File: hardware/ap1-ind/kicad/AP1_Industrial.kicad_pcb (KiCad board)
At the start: 2 copper layers, 88 x 56 mm, 71 parts, among them J1 ENTRADA 12-24V, J2 CONTACTORES, J3 0-10V, J7 PROGRAMADOR, Q1 AO3400A, Q2 AO3400A, U1 LMR16006XDDC, U2 B1212S-1WR3, U3 LM358DR2G, U4 LM358DR2G, U5 M24C02-WMN6TP

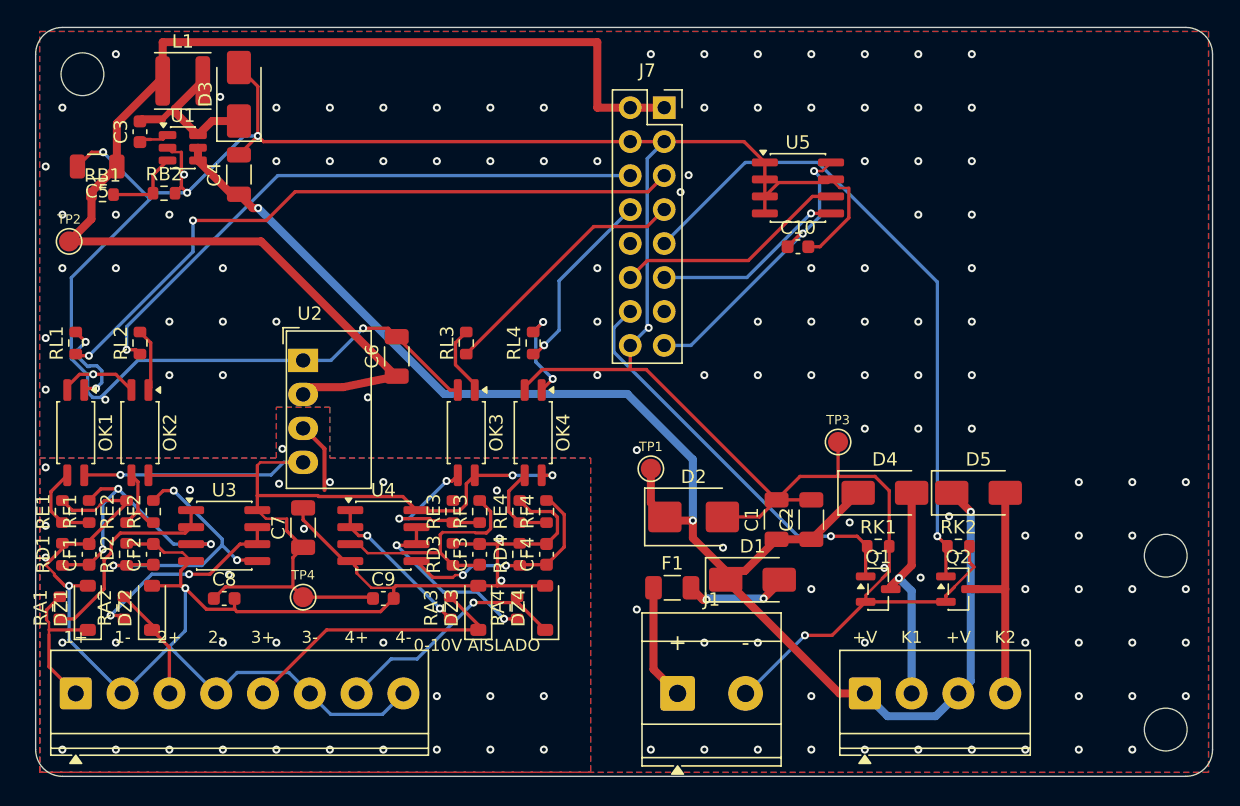
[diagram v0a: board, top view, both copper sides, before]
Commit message: Listo para JLCPCB: códigos LCSC, reglas de fabricación y carpeta de pedido
- Códigos LCSC verificados para todas las piezas SMD (INA238, LMR16006,
  UCC27524, AL8860, TMP1075, MOSFET, bobinas, capacitor, fusible, módulo,
  conectores) en tools/jlcpcb.py; piezas reconocidas por huella.
- Shunt: el WSK2512 de 4 terminales se agotó en LCSC; base y AP-0.2 usan un
  HoJLR2512 1 mOhm 2 W (C2924520) con huella propia 'net tie' que conserva
  el sensado Kelvin (tools/huellas/LetreroLab.pretty).
- ESP32-C3-WROOM-02: huella propia con 4 vías de 0.3 mm en lugar de 12 de
  0.2 mm (proceso estándar de JLCPCB). Textos de serigrafía de 0.8 mm o más.
- IND: fusible de 3 A (el mismo de la base).
- AP-0.2 ruteada otra vez con el nuevo shunt.
- Las 4 placas: ERC 0, DRC 0, 0 sin conectar, 0 diferencias y 0 problemas
  con las reglas de fabricación de JLCPCB.
- PEDIDO_JLCPCB/ (+ .zip) con Gerber, BOM y CPL completos o solo SMD por
  placa, y PEDIDO_JLCPCB.md con las opciones exactas del pedido.

Co-Authored-By: Claude Opus 5.5 <noreply@anthropic.com>
Claude-Session: https://claude.ai/code/session_01WVk3oGwfQfGTmAT2PMp8oW
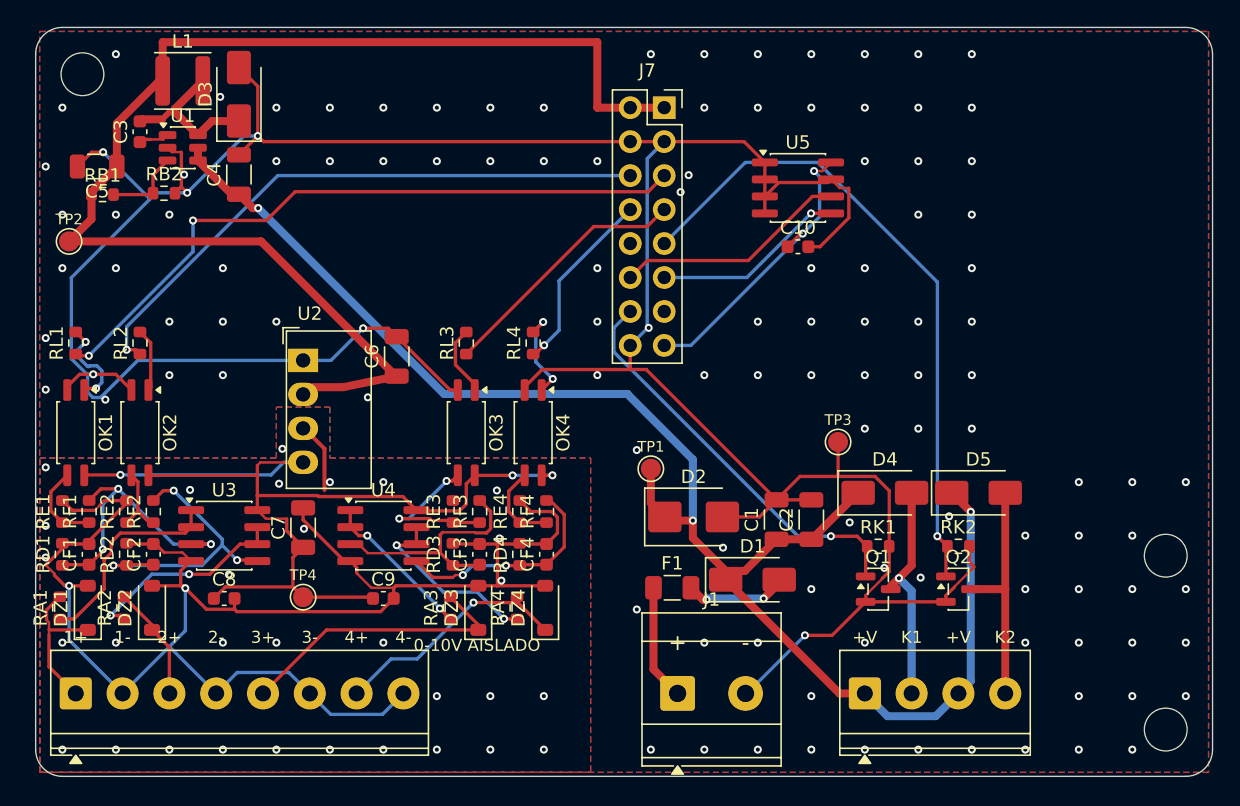
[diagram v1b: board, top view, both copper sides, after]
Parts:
- F1: value 2A -> 3A
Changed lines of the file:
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@@
 			)
 		)
-		(property "Value" "2A"
+		(property "Value" "3A"
 			(at 0 1.83 0)
 			(layer "F.Fab")
@@
 			(effects
 				(font
-					(size 0.7 0.7)
-					(thickness 0.12)
+					(size 0.8 0.8)
+					(thickness 0.15)
 				)
 			)
@@
 			(effects
 				(font
-					(size 0.7 0.7)
-					(thickness 0.12)
+					(size 0.8 0.8)
+					(thickness 0.15)
 				)
 			)
@@
 			(effects
 				(font
-					(size 0.7 0.7)
-					(thickness 0.12)
+					(size 0.8 0.8)
+					(thickness 0.15)
 				)
 			)
@@
 			(effects
 				(font
-					(size 0.7 0.7)
-					(thickness 0.12)
+					(size 0.8 0.8)
+					(thickness 0.15)
 				)
 			)

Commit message: AP CONNECT: sin borneras en todas las placas, placa nueva AP PRO AI4 y guía de fabricantes
- Borneras de tornillo reemplazadas por conectores con cable y código LCSC verificado:
  XT60 (C98732), JST VH 2/3/4 (C160315/6/7), JST XH 2/3/4 (C158012, C144394/5), Qwiic
  en BASE, IND, PIX, DMX, PLANTILLA, AP INPUT, AP OUTPUT y DIST 4; zonas de potencia rehechas
- XT60 de la DIST 4 con la polaridad marcada en la huella (pata 1 = -, pata 2 = +)
- TCA9554PWR ya con código (C477924)
- ap1-ai4: 4 entradas 0-10 V / 4-20 mA con ADS1115 (C37593), +24 V para sensores de lazo
- Programa 1.7: lectura AI4, umbrales con acciones, Home Assistant, tarjeta en la app
- FABRICANTES.md: JLCPCB, PCBWay, Seeed, NextPCB, México; impresión 3D y tornillería
- Pedido JLCPCB con 10 placas (AP-0.2 retirada); ERC/DRC/DFM 0 en todas

Co-Authored-By: Claude Opus 5.5 <noreply@anthropic.com>
Claude-Session: https://claude.ai/code/session_01WVk3oGwfQfGTmAT2PMp8oW
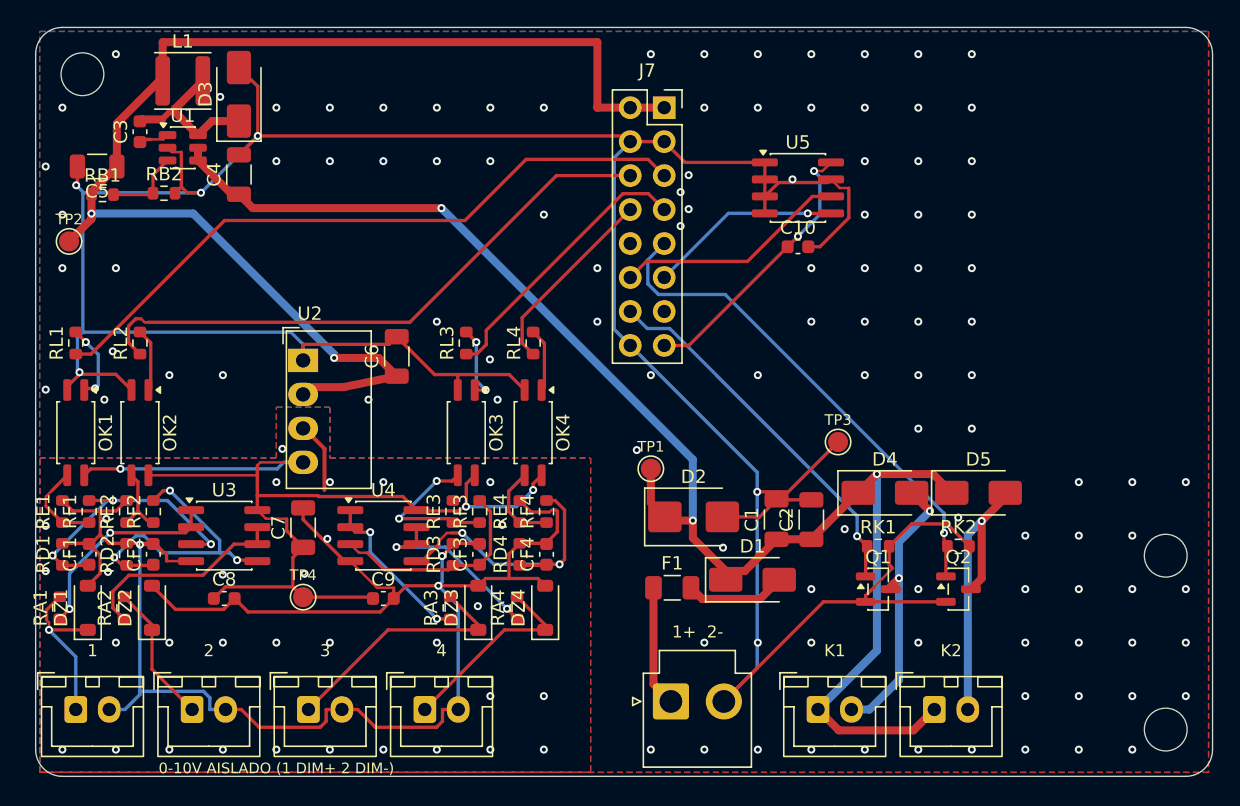
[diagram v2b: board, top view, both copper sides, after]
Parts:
- removed J3: 0-10V, TerminalBlock_Phoenix:TerminalBlock_Phoenix_PT-1,5-8-3.5-H_1x08_P3.50mm_Horizontal
- added J4: K2, Connector_JST:JST_XH_B2B-XH-A_1x02_P2.50mm_Vertical, F.Cu at (167.2, 151.0)
- added J5: 0-10V 1, Connector_JST:JST_XH_B2B-XH-A_1x02_P2.50mm_Vertical, F.Cu at (103.0, 151.0)
- added J6: 0-10V 2, Connector_JST:JST_XH_B2B-XH-A_1x02_P2.50mm_Vertical, F.Cu at (111.7, 151.0)
- added J8: 0-10V 3, Connector_JST:JST_XH_B2B-XH-A_1x02_P2.50mm_Vertical, F.Cu at (120.4, 151.0)
- added J9: 0-10V 4, Connector_JST:JST_XH_B2B-XH-A_1x02_P2.50mm_Vertical, F.Cu at (129.1, 151.0)
- J1: footprint TerminalBlock_Phoenix:TerminalBlock_Phoenix_MKDS-3-2-5.08_1x02_P5.08mm_Horizontal -> Connector_JST:JST_VH_B2P-VH_1x02_P3.96mm_Vertical
- J2: value CONTACTORES -> K1; footprint TerminalBlock_Phoenix:TerminalBlock_Phoenix_PT-1,5-4-3.5-H_1x04_P3.50mm_Horizontal -> Connector_JST:JST_XH_B2B-XH-A_1x02_P2.50mm_Vertical
- moved J2 3.70 mm to (158.5, 151.0)
- moved J1 0.78 mm to (147.5, 150.4)
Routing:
- net /CC1: track 49.0 -> 37.6 mm
- net /ISOGND: track 129.9 -> 140.2 mm, vias 33 -> 35
- net /GND: track 234.6 -> 240.5 mm, vias 119 -> 112
- net /K2: track 17.6 -> 22.8 mm, vias 0 -> 1
- net /FL4: track 16.7 -> 21.6 mm
- net /K1: track 16.9 -> 21.1 mm, vias 1 -> 2
- net /DIM4: track 18.2 -> 14.8 mm, vias 1 -> 0
- net /DIM3: track 21.4 -> 18.5 mm
- net /AUX: track 30.8 -> 28.2 mm
- net /LA4: track 7.25 -> 4.77 mm, vias 2 -> 0
- net /FL3: track 18.2 -> 16.1 mm
- net /DIM2: track 8.63 -> 10.5 mm
- net /3V3: track 22.3 -> 20.7 mm
- net /PWM3: track 19.3 -> 20.9 mm
- net /LA1: track 7.13 -> 5.87 mm
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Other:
- board text added: "0-10V AISLADO (1 DIM+ 2 DIM-)"
- board text added: "1"
- board text added: "1+ 2-"
- board text added: "2"
- board text added: "3"
- board text added: "4"
- board text removed: "+"
- board text removed: "+V"
- board text removed: "-"
- board text removed: "0-10V AISLADO"
- board text removed: "1+"
- board text removed: "1-"
- board text removed: "2+"
- board text removed: "2-"
- board text removed: "3+"
- board text removed: "3-"
- board text removed: "4+"
- board text removed: "4-"
